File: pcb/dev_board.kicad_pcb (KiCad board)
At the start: 6 copper layers, 69.2 x 41.2 mm, 29 parts, among them J1 Conn_02x13_Odd_Even, J2 Conn_02x13_Odd_Even, SW1 SW_DIP_x03, SW2 ARM, U1 LPC, U2 MCP3202, U3 TLV74325, U4 TLV74318, U5 LPC, U6 TLV74318

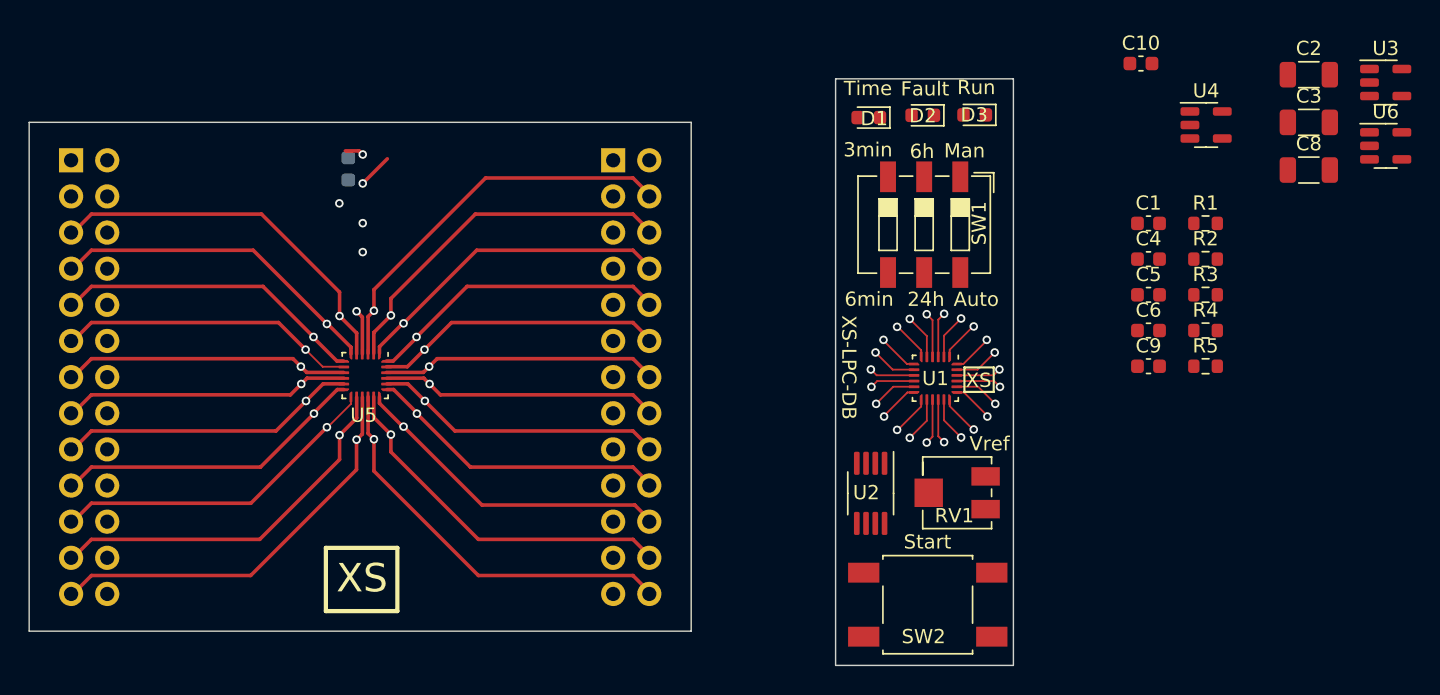
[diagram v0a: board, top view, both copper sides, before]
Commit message: V0.1 schematic complete, pcb placed. emulator connections, 24-stqfn LPC fanout in place.
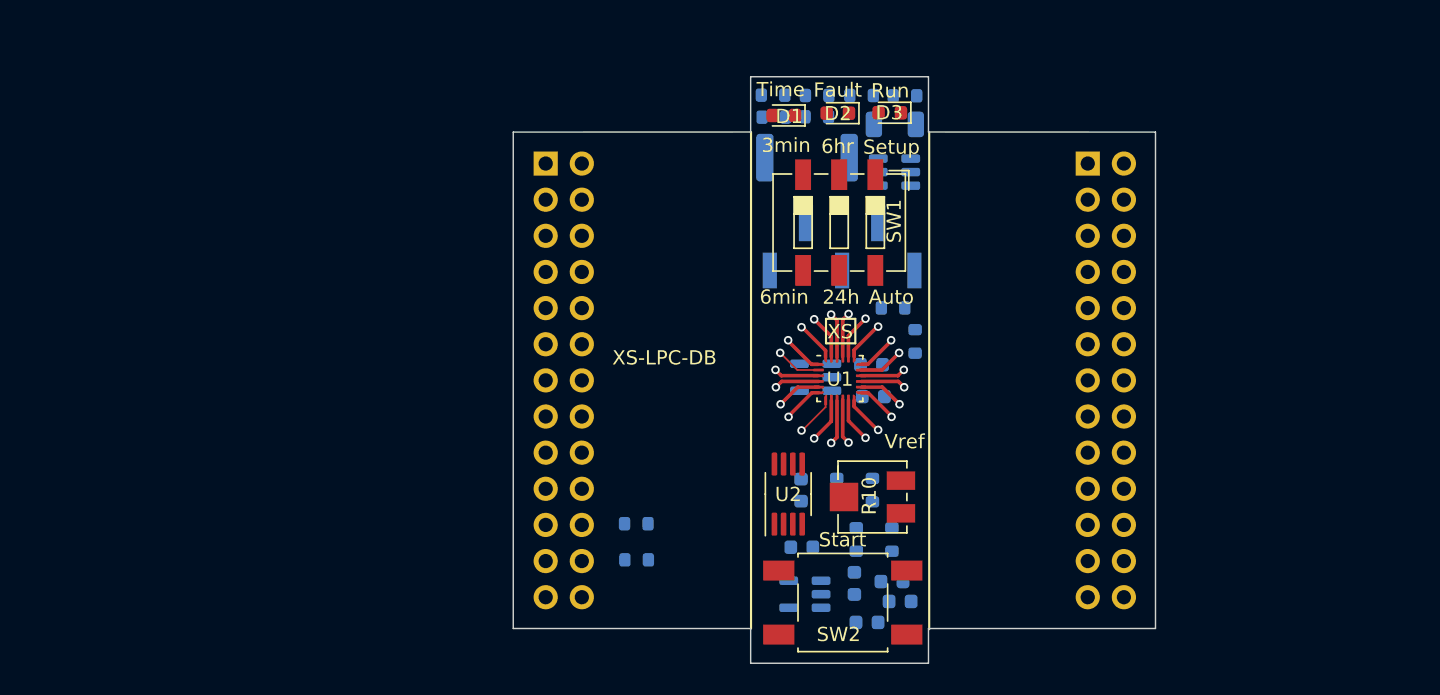
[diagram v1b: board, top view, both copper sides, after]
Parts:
- removed C2: 4.7u, Capacitor_SMD:C_1206_3216Metric
- removed RV1: R_Potentiometer_US, Potentiometer_SMD:Potentiometer_Bourns_3224J_Horizontal
- removed U4: TLV74318, Package_TO_SOT_SMD:SOT-23-5
- removed U5: LPC, myspace pcb:QFN-24-3x3mm
- added D6: DT1042-04SO-7, Package_TO_SOT_SMD:SOT-23-6, B.Cu at (163.9, 98.9)
- added J4: Conn_01x05, Connector_PinHeader_2.54mm:PinHeader_1x05_P2.54mm_Vertical_SMD_Pin1Left, B.Cu at (160.2, 104.1)
- added R10: 1K5, Potentiometer_SMD:Potentiometer_Bourns_3224J_Horizontal, F.Cu at (162.4, 121.7)
- added R11: 47, Resistor_SMD:R_0603_1608Metric, B.Cu at (161.2, 124.7)
- added R12: 47, Resistor_SMD:R_0603_1608Metric, B.Cu at (163.7, 124.7)
- added R13: 47, Resistor_SMD:R_0603_1608Metric, B.Cu at (155.4, 95.0)
- added R14: 47, Resistor_SMD:R_0603_1608Metric, B.Cu at (155.4, 93.5)
- added R15: 1R 3W 0.1%, Resistor_SMD:R_2512_6332Metric, B.Cu at (157.8, 97.9)
- added R16: 47, Resistor_SMD:R_0603_1608Metric, B.Cu at (158.4, 95.0)
- added R6: 1K, Resistor_SMD:R_0603_1608Metric, B.Cu at (163.8, 108.4)
- added R7: 1K5, Resistor_SMD:R_0603_1608Metric, B.Cu at (159.8, 121.2)
- added R8: 18R6, Resistor_SMD:R_0603_1608Metric, B.Cu at (162.4, 121.2)
- added R9: 3k3, Resistor_SMD:R_0603_1608Metric, B.Cu at (165.4, 110.8)
- C1, C10, C4, C8, C9, R2, R3, R4: moved to B.Cu
- C3: value 4.7u -> 22n; footprint Capacitor_SMD:C_1206_3216Metric -> Capacitor_SMD:C_0603_1608Metric; moved to B.Cu
- C5, C6: value 1u -> 22n; moved to B.Cu
- D1: value Yel -> RUN
- D2: value Yel -> FLT
- D3: value Yel -> TME
- R1: value 10K -> 0R; moved to B.Cu
- R5: value 10K -> DNI; moved to B.Cu
- U3: value TLV74325 -> TLV75530PDBV; moved to B.Cu
- U6: value TLV74318 -> TLV74311; moved to B.Cu
- moved U3 54.4 mm to (157.6, 128.5), turned to 180 degrees
- moved R1 46.5 mm to (145.8, 126.1), turned to 180 degrees
- moved C7 46.0 mm to (161.1, 127.8)
- moved C3 43.6 mm to (163.7, 127.7), turned to 180 degrees
- moved U6 43.2 mm to (158.4, 113.3), turned to 180 degrees
- moved R5 41.5 mm to (145.8, 123.6), turned to 180 degrees
- moved J2 33.4 mm to (177.5, 98.3)
- moved J1 33.4 mm to (139.4, 98.3)
- moved C4 32.3 mm to (162.0, 130.5), turned to 180 degrees
- moved C1 30.8 mm to (157.3, 121.2), turned to -90 degrees
- moved C5 30.1 mm to (157.4, 125.2), turned to 180 degrees
- moved R2 29.6 mm to (158.5, 93.5)
- moved C8 29.3 mm to (163.9, 95.5)
- moved C10 28.4 mm to (162.3, 112.4), turned to 180 degrees
- moved R3 27.9 mm to (161.6, 93.5)
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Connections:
- net /dataA1 renamed Net-(J2-Pin_17)
- net /dataB0 renamed Net-(J2-Pin_15)
- net /mute_n renamed /pump
- C1 pad 1: +3.3V -> /CT2
- C3 pad 1: +3.3V -> /CT2
- C5 pad 1: +3.3V -> Net-(U2-CH1)
- C6 pad 1: +1V1 -> Net-(U2-CH0)
- C7 pad 1: +2V5 -> +3V0
- D1 pad 2: unconnected-(D1-A-Pad2) -> /run_led
- D2 pad 2: unconnected-(D2-A-Pad2) -> /fault_led
- D3 pad 2: unconnected-(D3-A-Pad2) -> /time_led
- J1 pad 20: /speaker -> /start
- J1 pad 24: /reset_n -> Net-(J1-Pin_24)
- J1 pad 6: /charge -> /run_led
- J2 pad 11: /sclk -> /timeout
- J2 pad 13: /dataA0 -> /time_led
- J2 pad 19: /dataB1 -> /adc_clk
- J2 pad 21: /cs -> /adc_miso
- J2 pad 23: /pwm -> /adc_mosi
- J2 pad 25: /arm_led -> /adc_ncs
- J2 pad 5: /cont_led -> /setup
- J2 pad 7: /launch_n -> /fault_led
- J2 pad 9: /dump -> /period
- R1 pad 1: +3.3V -> Net-(J1-Pin_24)
- R1 pad 2: Net-(U3-EN) -> /reset_n
- R2 pad 2: unconnected-(R2-Pad2) -> GND
- R3 pad 2: unconnected-(R3-Pad2) -> GND
- R4 pad 2: unconnected-(R4-Pad2) -> GND
- R5 pad 1: +3.3V -> GND
- R5 pad 2: Net-(U6-EN) -> /reset_n
- SW1 pad 4: unconnected-(SW1-Pad4) -> /timeout
- SW1 pad 5: unconnected-(SW1-Pad5) -> /period
- SW1 pad 6: unconnected-(SW1-Pad6) -> /setup
- SW2 pad 1: unconnected-(SW2-Pad1) -> GND
- SW2 pad 2: unconnected-(SW2-Pad2) -> /start
- U1 pad 1: /dump -> /period
- U1 pad 13: /speaker -> /start
- U1 pad 2: /sclk -> /timeout
- U1 pad 20: /charge -> /run_led
- U1 pad 23: /cont_led -> /setup
- U1 pad 24: /launch_n -> /fault_led
- U1 pad 3: /dataA0 -> /time_led
- U1 pad 6: /dataB1 -> /adc_clk
- U1 pad 7: /cs -> /adc_miso
- U1 pad 8: /pwm -> /adc_mosi
- U1 pad 9: /arm_led -> /adc_ncs
- U2 pad 1: unconnected-(U2-~{CS}/SHDN-Pad1) -> /adc_ncs
- U2 pad 2: unconnected-(U2-CH0-Pad2) -> Net-(U2-CH0)
- U2 pad 3: unconnected-(U2-CH1-Pad3) -> Net-(U2-CH1)
- U2 pad 4: unconnected-(U2-VSS-Pad4) -> GND
- U2 pad 5: unconnected-(U2-DIN-Pad5) -> /adc_mosi
- U2 pad 6: unconnected-(U2-DOUT-Pad6) -> /adc_miso
- U2 pad 7: unconnected-(U2-CLK-Pad7) -> /adc_clk
- U2 pad 8: unconnected-(U2-VDD/VREF-Pad8) -> +3V0
- U3 pad 3: Net-(U3-EN) -> +3.3V
- U3 pad 5: +2V5 -> +3V0
- U6 pad 3: Net-(U6-EN) -> +3.3V
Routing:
- net GND: track 535.7 -> 2.84 mm, vias 27 -> 1
- net Net-(J2-Pin_15): track 6.34 -> 3.17 mm, vias 2 -> 1
- net /time_led: track 0.00 -> 3.17 mm, vias 0 -> 1
- net /dataA0: track 3.17 -> 0.00 mm, vias 1 -> 0
- net /arm_led: track 3.17 -> 0.00 mm, vias 1 -> 0
- net /adc_ncs: track 0.00 -> 3.17 mm, vias 0 -> 1
- net /pwm: track 3.17 -> 0.00 mm, vias 1 -> 0
- net /charge: track 3.17 -> 0.00 mm, vias 1 -> 0
- net /cont_led: track 3.17 -> 0.00 mm, vias 1 -> 0
- net /sclk: track 3.17 -> 0.00 mm, vias 1 -> 0
- net /adc_mosi: track 0.00 -> 3.17 mm, vias 0 -> 1
- net /setup: track 0.00 -> 3.17 mm, vias 0 -> 1
- net /run_led: track 0.00 -> 3.17 mm, vias 0 -> 1
- net /timeout: track 0.00 -> 3.17 mm, vias 0 -> 1
- net /start: track 0.00 -> 2.84 mm, vias 0 -> 1
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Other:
- board size 69.2 x 41.2 mm -> 45.1 x 41.2 mm
- board text added: "6hr"
- board text added: "Setup"
- board text removed: "6h"
- board text removed: "Man"
